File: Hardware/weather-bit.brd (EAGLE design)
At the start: 68.6 x 58.4 mm, 73 parts, among them J10 SMD, J2 RJ11, J3 RJ11, J8 Qwiic (vertical), J9 SMD, U1 BME280, U2 micro:bit

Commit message: run of checklist
- vector font in sch
- added testpoints
- corrected measures
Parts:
- added TP1, TP13, TP14, TP19, TP2, TP3, TP4, TP5, TP8, TP9: (no value), SparkFun-Connectors:TP_15TH
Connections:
- removed net 10: U2.P$16
- removed net 11: U2.P$17
- removed net 3: U2.P$1
- removed net 4: U2.P$6
- removed net 5: U2.P$7
- removed net 6: U2.P$8
- removed net 7: U2.P$9
- removed net 9: U2.P$15
- removed net N$3: U2.P$23
- net 3.3V: now also TP1.P$1
- net GND: now also TP2.P$1
- net RAIN: now also TP8.P$1
- net SCL: now also TP4.P$1
- net SDA: now also TP3.P$1
- net SOIL_DAT: now also TP19.P$1
- net SOIL_PWR: now also TP5.P$1
- net TEMP_DAT: now also TP9.P$1
- net WDIR: now also TP14.P$1
- net WSPEED: now also TP13.P$1
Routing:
- net SOIL_DAT: track 67.0 -> 77.2 mm
- net SCL: track 36.2 -> 44.2 mm
- net SDA: track 36.9 -> 43.8 mm
- net SOIL_PWR: track 52.9 -> 57.3 mm
- net TEMP_DAT: track 60.7 -> 65.1 mm
- net WSPEED: track 53.9 -> 57.8 mm
- net WDIR: track 50.2 -> 54.0 mm
- net RAIN: track 51.7 -> 55.6 mm
- net 3.3V: track 196.1 -> 200.0 mm
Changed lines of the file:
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@@
 <text x="31.75" y="-11.43" size="1.778" layer="51" font="vector" ratio="9">Mary West, based on Weather Shield Design by Nathan Seidle </text>
 <text x="67.16395" y="18.07845" size="1.778" layer="16" font="vector" ratio="15" rot="SMR270" align="center">v11</text>
-<text x="30.63875" y="90.4875" size="1.778" layer="47" font="vector" ratio="15">* All dimensions
+<text x="30.63875" y="81.5975" size="1.778" layer="47" font="vector" ratio="15">* All dimensions
   are in inches</text>
 <wire x1="2.54" y1="58.42" x2="66.04" y2="58.42" width="0.2032" layer="20"/>
@@
 <wire x1="68.58" y1="55.88" x2="68.58" y2="2.54" width="0.2032" layer="20"/>
 <wire x1="2.54" y1="58.42" x2="0" y2="55.88" width="0.2032" layer="20" curve="90"/>
-<dimension x1="68.58" y1="2.54" x2="68.58" y2="67.31" x3="85.09" y3="34.925" textsize="1.778" layer="47" unit="inch"/>
-<dimension x1="68.58" y1="67.31" x2="0" y2="67.31" x3="34.29" y3="81.5975" textsize="1.778" layer="47" unit="inch"/>
+<dimension x1="68.58" y1="2.54" x2="68.58" y2="58.42" x3="85.09" y3="30.48" textsize="1.778" layer="47" unit="inch"/>
+<dimension x1="68.58" y1="58.42" x2="0" y2="58.42" x3="34.29" y3="72.7075" textsize="1.778" layer="47" unit="inch"/>
 <wire x1="43.60545" y1="36.2204" x2="43.60545" y2="31.8516" width="0.254" layer="21"/>
 <wire x1="43.60545" y1="31.8516" x2="50.64125" y2="31.877" width="0.254" layer="21"/>
@@
 <wire x1="2.54" y1="0" x2="0" y2="2.54" width="0.2032" layer="20" curve="-90"/>
 <wire x1="0" y1="2.54" x2="0" y2="55.88" width="0.2032" layer="20"/>
-<dimension x1="2.54" y1="64.77" x2="66.04" y2="64.77" x3="34.29" y3="73.3425" textsize="1.778" textratio="15" layer="47" unit="inch"/>
-<dimension x1="66.04" y1="64.77" x2="66.04" y2="2.54" x3="75.2475" y3="33.655" textsize="1.778" textratio="15" layer="47" unit="inch"/>
+<dimension x1="2.54" y1="55.88" x2="66.04" y2="55.88" x3="34.29" y3="64.4525" textsize="1.778" textratio="15" layer="47" unit="inch"/>
+<dimension x1="66.04" y1="55.88" x2="66.04" y2="2.54" x3="75.2475" y3="29.21" textsize="1.778" textratio="15" layer="47" unit="inch"/>
 <dimension x1="66.04" y1="2.54" x2="67.78625" y2="2.54" x3="66.913125" y3="-2.06375" textsize="1.778" layer="47" unit="inch"/>
-<dimension x1="2.54" y1="64.77" x2="0.79375" y2="64.77" x3="1.666875" y3="69.5325" textsize="1.778" layer="47" unit="inch"/>
+<dimension x1="2.54" y1="55.88" x2="0.79375" y2="55.88" x3="1.666875" y3="60.6425" textsize="1.778" layer="47" unit="inch"/>
 <text x="6.223" y="-32.385" size="2.54" layer="51">Solder Mask: Black Gloss</text>
 <text x="11.43" y="-13.97" size="1.778" layer="51" font="vector">Revised by:</text>
@@
 <element name="U$33" library="buzzard_labels" package="SPARKFUN#COM#MICROBIT17" value="" x="49.1744" y="15.7226" smashed="yes" rot="MR0"/>
 <element name="U$34" library="buzzard_labels (1)" package="ALT0" value="" x="51.6382" y="36.3728" smashed="yes" rot="R270"/>
+<element name="TP1" library="SparkFun-Connectors" package="TP_15TH" value="" x="41.91" y="49.53" smashed="yes" rot="R90"/>
+<element name="TP2" library="SparkFun-Connectors" package="TP_15TH" value="" x="49.53" y="49.53" smashed="yes" rot="R90"/>
+<element name="TP3" library="SparkFun-Connectors" package="TP_15TH" value="" x="46.99" y="49.53" smashed="yes" rot="R90"/>
+<element name="TP4" library="SparkFun-Connectors" package="TP_15TH" value="" x="44.45" y="49.53" smashed="yes" rot="R90"/>
+<element name="TP5" library="SparkFun-Connectors" package="TP_15TH" value="" x="39.37" y="49.53" smashed="yes" rot="R90"/>
+<element name="TP8" library="SparkFun-Connectors" package="TP_15TH" value="" x="31.75" y="49.53" smashed="yes" rot="R90"/>
+<element name="TP9" library="SparkFun-Connectors" package="TP_15TH" value="" x="29.21" y="49.53" smashed="yes" rot="R90"/>
+<element name="TP13" library="SparkFun-Connectors" package="TP_15TH" value="" x="26.67" y="49.53" smashed="yes" rot="R90"/>
+<element name="TP14" library="SparkFun-Connectors" package="TP_15TH" value="" x="24.13" y="49.53" smashed="yes" rot="R90"/>
+<element name="TP19" library="SparkFun-Connectors" package="TP_15TH" value="" x="21.59" y="49.53" smashed="yes" rot="R90"/>
 </elements>
 <signals>
@@
 <wire x1="4.7234" y1="30.3022" x2="1.4234" y2="30.3022" width="0.254" layer="1"/>
 <wire x1="1.4234" y1="30.3022" x2="1.4234" y2="27.7622" width="0.254" layer="1"/>
+<contactref element="TP2" pad="P$1"/>
 </signal>
 <signal name="3.3V">
@@
 <wire x1="54.5976" y1="33.1678" x2="49.73405" y2="33.1678" width="0.508" layer="1"/>
 <wire x1="49.70145" y1="33.1352" x2="49.73405" y2="33.1678" width="0.508" layer="1"/>
+<contactref element="TP1" pad="P$1"/>
+<wire x1="42.545" y1="45.92" x2="42.545" y2="48.895" width="0.2032" layer="1"/>
+<wire x1="42.545" y1="48.895" x2="41.91" y2="49.53" width="0.2032" layer="1"/>
 </signal>
 <signal name="N$2">
@@
 <wire x1="63.8312" y1="32.0294" x2="63.7794" y2="32.0294" width="0.254" layer="1"/>
 <wire x1="63.7794" y1="32.0294" x2="63.641" y2="32.1678" width="0.254" layer="1"/>
+<contactref element="TP3" pad="P$1"/>
+<wire x1="51.435" y1="45.92" x2="51.435" y2="47.625" width="0.2032" layer="1"/>
+<wire x1="51.435" y1="47.625" x2="50.8" y2="48.26" width="0.2032" layer="1"/>
+<wire x1="50.8" y1="48.26" x2="48.26" y2="48.26" width="0.2032" layer="1"/>
+<wire x1="48.26" y1="48.26" x2="46.99" y2="49.53" width="0.2032" layer="1"/>
 </signal>
 <signal name="SCL">
@@
 <wire x1="67.1312" y1="30.227" x2="66.9036" y2="30.4546" width="0.254" layer="1"/>
 <wire x1="66.9036" y1="30.4546" x2="60.9854" y2="30.4546" width="0.254" layer="1"/>
+<contactref element="TP4" pad="P$1"/>
+<wire x1="50.165" y1="45.92" x2="50.165" y2="47.3456" width="0.2032" layer="1"/>
+<wire x1="49.8094" y1="47.7012" x2="46.2788" y2="47.7012" width="0.2032" layer="1"/>
+<wire x1="46.2788" y1="47.7012" x2="44.45" y2="49.53" width="0.2032" layer="1"/>
+<wire x1="50.165" y1="47.3456" x2="49.8094" y2="47.7012" width="0.2032" layer="1"/>
 </signal>
 <signal name="N$5">
@@
 <wire x1="32.0675" y1="24.765" x2="31.115" y2="25.7175" width="0.254" layer="1"/>
 <wire x1="31.115" y1="25.7175" x2="31.115" y2="45.92" width="0.254" layer="1"/>
+<contactref element="TP9" pad="P$1"/>
+<wire x1="31.115" y1="45.92" x2="31.115" y2="47.625" width="0.2032" layer="1"/>
+<wire x1="31.115" y1="47.625" x2="29.21" y2="49.53" width="0.2032" layer="1"/>
 </signal>
 <signal name="SOIL_PWR">
@@
 <contactref element="U2" pad="P$26"/>
 <wire x1="41.275" y1="45.92" x2="41.275" y2="42.8625" width="0.254" layer="1"/>
+<contactref element="TP5" pad="P$1"/>
+<wire x1="41.275" y1="45.92" x2="41.275" y2="47.625" width="0.2032" layer="1"/>
+<wire x1="41.275" y1="47.625" x2="39.37" y2="49.53" width="0.2032" layer="1"/>
 </signal>
 <signal name="SOIL_DAT">
@@
 <wire x1="12.065" y1="43.815" x2="13.335" y2="43.815" width="0.254" layer="1"/>
 <wire x1="12.065" y1="45.92" x2="12.065" y2="43.815" width="0.254" layer="1"/>
+<contactref element="TP19" pad="P$1"/>
+<wire x1="14.605" y1="45.92" x2="14.605" y2="48.895" width="0.2032" layer="1"/>
+<wire x1="14.605" y1="48.895" x2="15.24" y2="49.53" width="0.2032" layer="1"/>
+<wire x1="15.24" y1="49.53" x2="21.59" y2="49.53" width="0.2032" layer="1"/>
 </signal>
 <signal name="RAIN">
@@
 <wire x1="33.655" y1="45.92" x2="33.655" y2="43.688" width="0.254" layer="1"/>
 <wire x1="34.925" y1="45.92" x2="34.925" y2="43.688" width="0.254" layer="1"/>
+<contactref element="TP8" pad="P$1"/>
+<wire x1="32.385" y1="45.92" x2="32.385" y2="48.895" width="0.2032" layer="1"/>
+<wire x1="32.385" y1="48.895" x2="31.75" y2="49.53" width="0.2032" layer="1"/>
 </signal>
 <signal name="WDIR">
@@
 <wire x1="22.225" y1="45.92" x2="22.225" y2="43.7261" width="0.254" layer="1"/>
 <wire x1="23.495" y1="45.92" x2="23.495" y2="43.7261" width="0.254" layer="1"/>
+<contactref element="TP14" pad="P$1"/>
+<wire x1="24.765" y1="45.92" x2="24.765" y2="48.895" width="0.2032" layer="1"/>
+<wire x1="24.765" y1="48.895" x2="24.13" y2="49.53" width="0.2032" layer="1"/>
 </signal>
 <signal name="WSPEED">
@@
 <wire x1="17.78" y1="21.17" x2="17.78" y2="22.5425" width="0.254" layer="1"/>
 <wire x1="17.78" y1="22.5425" x2="18.0975" y2="22.86" width="0.254" layer="1"/>
-<wire x1="26.44775" y1="22.86" x2="26.67" y2="22.86" width="0.254" layer="1"/>
-<wire x1="26.67" y1="22.86" x2="38.1" y2="22.86" width="0.254" layer="1"/>
+<wire x1="26.035" y1="22.86" x2="38.1" y2="22.86" width="0.254" layer="1"/>
 <wire x1="38.1" y1="22.86" x2="40.64" y2="22.86" width="0.254" layer="1"/>
 <wire x1="40.64" y1="22.86" x2="41.91" y2="21.59" width="0.254" layer="1"/>
@@
 <contactref element="U2" pad="P$14"/>
 <wire x1="26.035" y1="45.92" x2="26.035" y2="22.86" width="0.254" layer="1"/>
-<wire x1="26.44775" y1="22.86" x2="26.035" y2="22.86" width="0.254" layer="1"/>
+<contactref element="TP13" pad="P$1"/>
+<wire x1="26.035" y1="45.92" x2="26.035" y2="48.895" width="0.2032" layer="1"/>
+<wire x1="26.035" y1="48.895" x2="26.67" y2="49.53" width="0.2032" layer="1"/>
 </signal>
 <signal name="N$1">
@@
 <wire x1="4.7234" y1="37.9222" x2="4.7244" y2="37.9212" width="0.254" layer="1"/>
 </signal>
-<signal name="11">
-<contactref element="U2" pad="P$17"/>
-</signal>
-<signal name="10">
-<contactref element="U2" pad="P$16"/>
-</signal>
-<signal name="7">
-<contactref element="U2" pad="P$9"/>
-</signal>
-<signal name="6">
-<contactref element="U2" pad="P$8"/>
-</signal>
-<signal name="5">
-<contactref element="U2" pad="P$7"/>
-</signal>
-<signal name="4">
-<contactref element="U2" pad="P$6"/>
-</signal>
-<signal name="3">
-<contactref element="U2" pad="P$1"/>
-</signal>
-<signal name="9">
-<contactref element="U2" pad="P$15"/>
-</signal>
-<signal name="N$3">
-<contactref element="U2" pad="P$23"/>
-</signal>
 </signals>

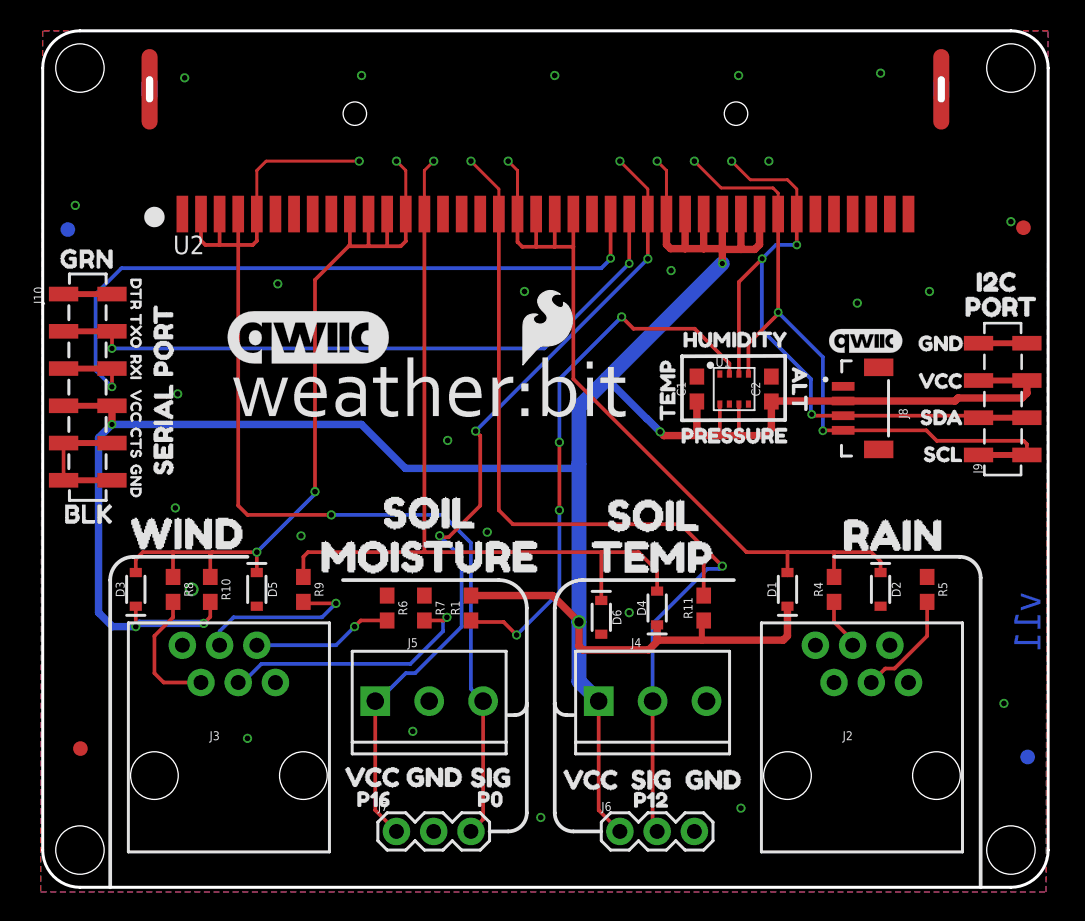
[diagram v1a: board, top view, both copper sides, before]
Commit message: switched to TIGHT DRC, nudging and routing
-updated package on 4-pin SMD to allow for routing to either pad under each header
-moved to TIGHT DRC, some slight nudging of routes to comply
-rotated SERIAL PORT silk to match pin labels
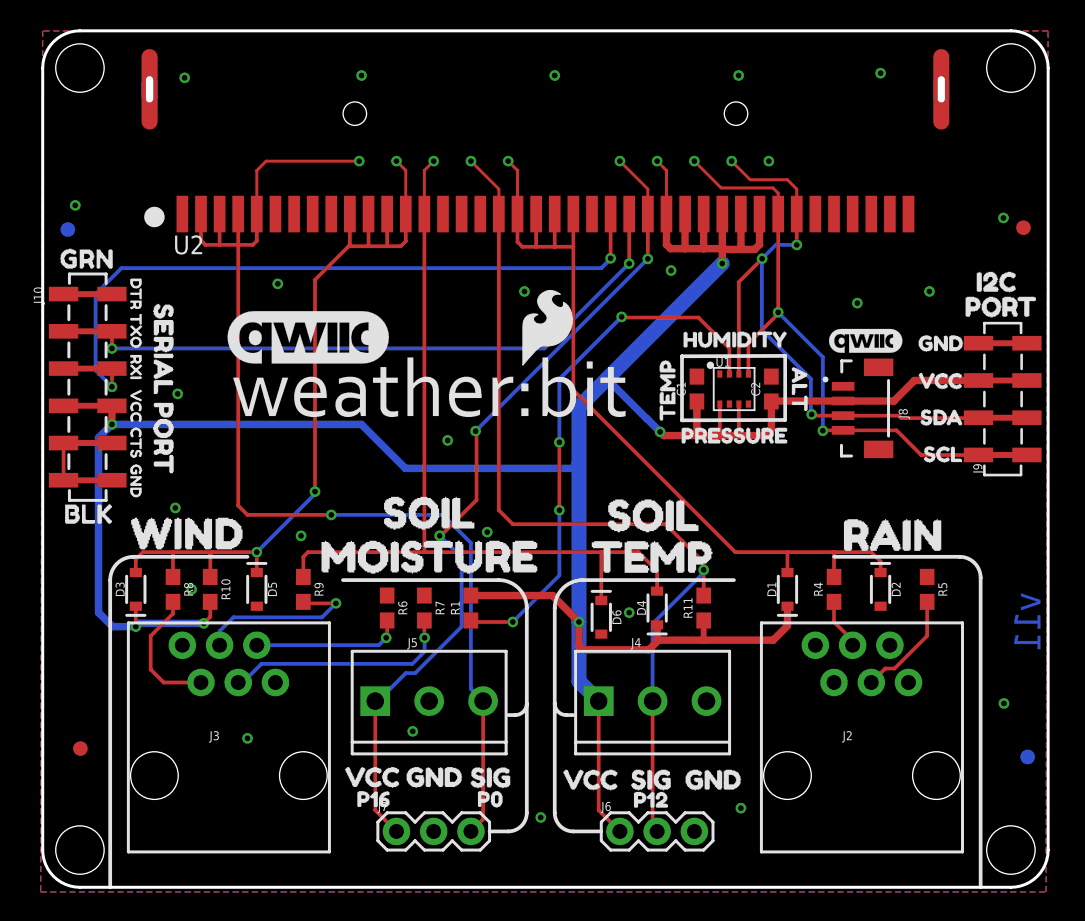
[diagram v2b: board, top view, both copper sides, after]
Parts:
- J9: value SMD -> 1X04_SMD_STRAIGHT_COMBO
- moved U$10 14.0 mm to (8.26, 40.9), turned to 270 degrees
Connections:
- net 3.3V: now also J9.3-2
- net GND: now also J9.4-2
- net SCL: now also J9.1-2
- net SDA: now also J9.2-2
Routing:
- net SDA: track 43.8 -> 47.2 mm
- net GND: track 5.84 -> 9.14 mm
- net TEMP_DAT: track 65.1 -> 61.8 mm
- net N$14: track 18.1 -> 15.7 mm
- net 3.3V: track 200.0 -> 198.9 mm
- net N$2: track 37.6 -> 36.8 mm
- net N$13: track 9.59 -> 10.2 mm
- net SOIL_PWR: track 57.3 -> 56.7 mm

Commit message: Finalized test points and test point positions
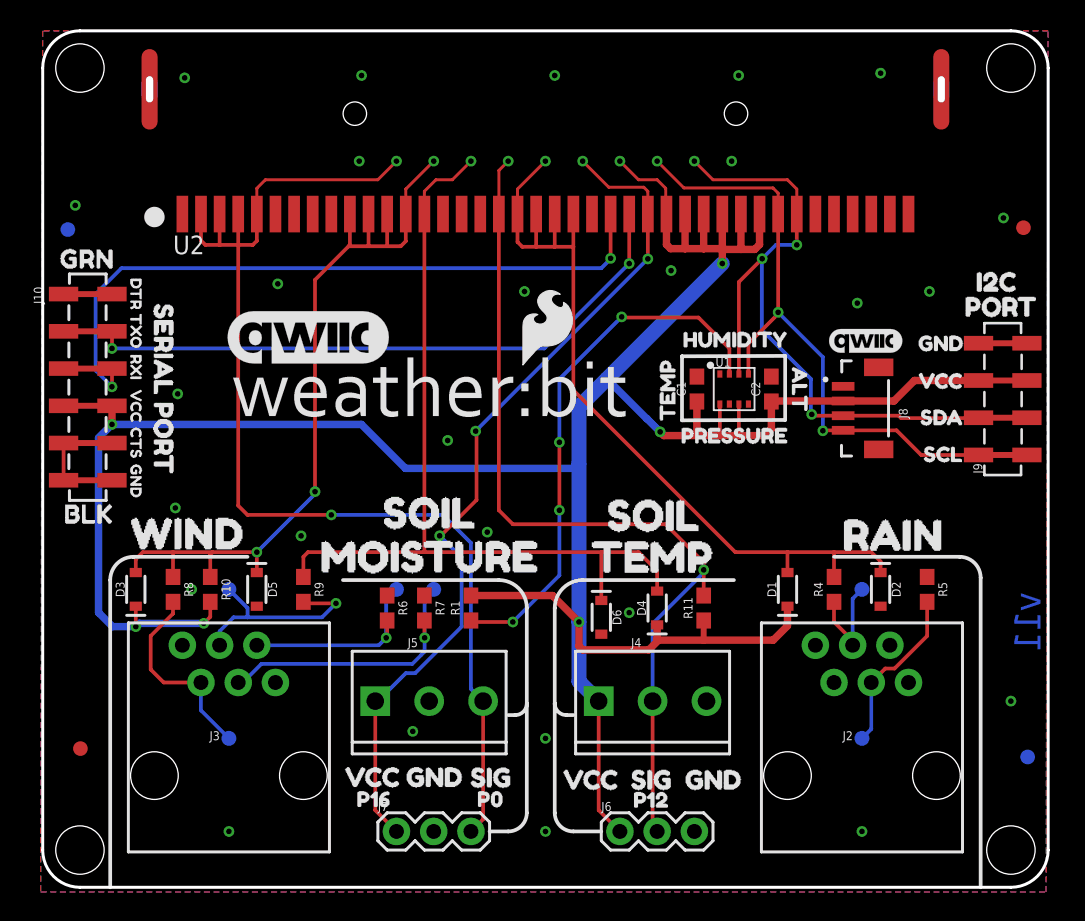
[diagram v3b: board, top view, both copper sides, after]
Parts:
- added TP10, TP11, TP12, TP15, TP6, TP7: (no value), SparkFun-Connectors:PAD.03X.04
- added TP16, TP17: (no value), SparkFun-Connectors:TP_15TH
- moved TP4 2.54 mm to (41.9, 49.5)
- moved TP14 2.54 mm to (26.7, 49.5)
- moved TP1 2.54 mm to (39.4, 49.5)
- moved TP13 2.54 mm to (29.2, 49.5)
- moved TP19 2.54 mm to (24.1, 49.5)
- moved TP2 2.54 mm to (47.0, 49.5)
- moved TP3 2.54 mm to (44.5, 49.5)
- moved TP5 2.54 mm to (36.8, 49.5)
- moved TP8 2.54 mm to (34.3, 49.5)
- moved TP9 2.54 mm to (31.8, 49.5)
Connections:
- removed net N$11: J3.3, R9.2
- removed net N$13: J3.5, R6.2
- removed net N$14: J3.4, R7.2
- removed net N$5: J2.3, R4.1
- removed net N$6: J3.2, R8.2
- removed net N$7: J2.4, R5.2
- new net RAIN_PIN_3: J2.3, R4.1, TP6.P$1
- new net RAIN_PIN_4: J2.4, R5.2, TP7.P$1
- new net WIND_PIN_2: J3.2, R8.2, TP10.P$1
- new net WIND_PIN_3: J3.3, R9.2, TP11.P$1
- new net WIND_PIN_4: J3.4, R7.2, TP12.P$1
- new net WIND_PIN_5: J3.5, R6.2, TP15.P$1
- net GND: now also TP16.P$1, TP17.P$1
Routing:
- net WIND_PIN_4: track 0.00 -> 19.3 mm, vias 0 -> 1
- net N$14: track 15.7 -> 0.00 mm, vias 1 -> 0
- net WIND_PIN_3: track 0.00 -> 14.4 mm, vias 0 -> 1
- net WIND_PIN_5: track 0.00 -> 13.8 mm, vias 0 -> 1
- net WIND_PIN_2: track 0.00 -> 13.6 mm
- net N$11: track 11.9 -> 0.00 mm, vias 1 -> 0
- net RAIN_PIN_4: track 0.00 -> 11.5 mm
- net N$13: track 10.2 -> 0.00 mm, vias 1 -> 0
- net N$6: track 9.04 -> 0.00 mm
- net RAIN_PIN_3: track 0.00 -> 7.56 mm
- net N$7: track 7.45 -> 0.00 mm
- net N$5: track 3.49 -> 0.00 mm
- net SDA: track 47.2 -> 49.7 mm
- net SCL: track 43.8 -> 46.3 mm
- net SOIL_PWR: track 56.7 -> 59.1 mm
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
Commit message: Connected TEMP_DATA to P13
On v10, TEMP_DATA was connected to both P12 and P13 (for the one-wire interface to the temp sensor).

v11 only had TEMP_DATA connected to P12.

With this commit (v12), TEMP_DATA is connected to both P12 and P13 (to match the original v10).

Also incremented version to v12 in BRD and SCH.
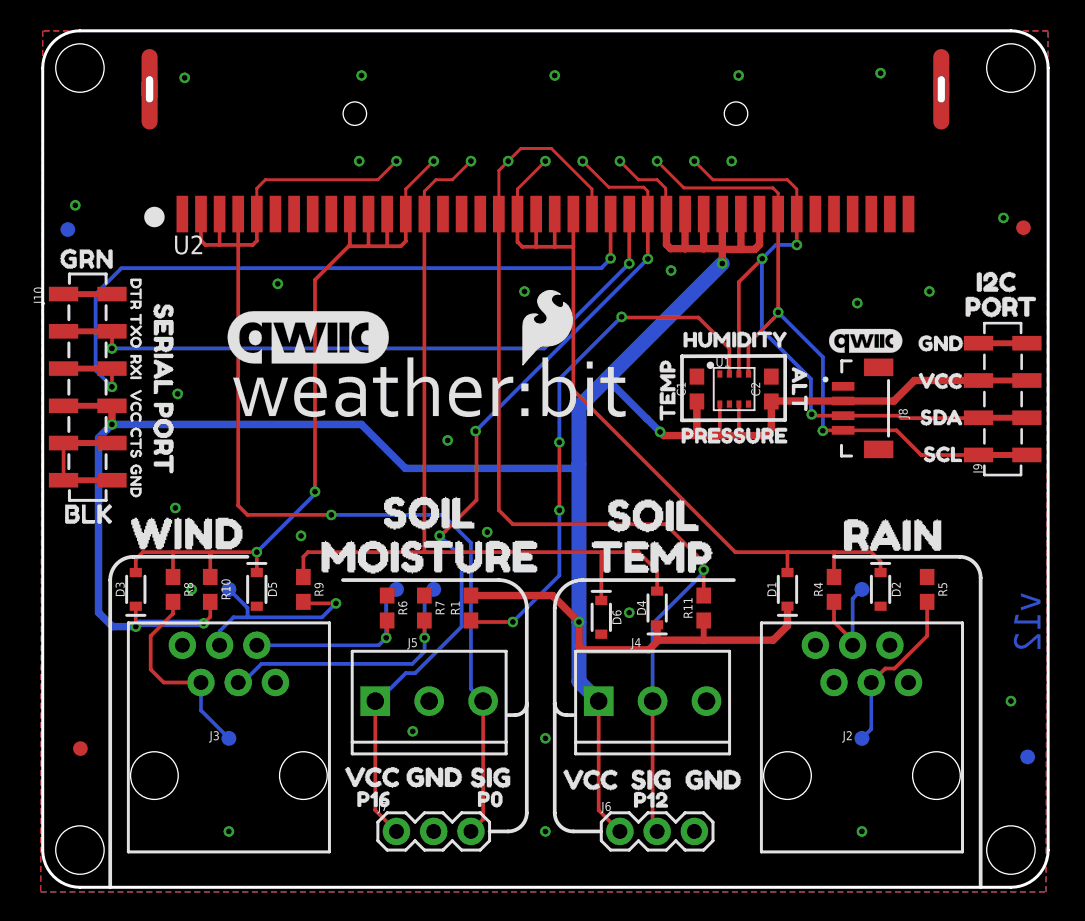
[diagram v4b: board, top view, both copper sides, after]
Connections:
- net TEMP_DAT: now also U2.P$23
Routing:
- net TEMP_DAT: track 61.3 -> 70.2 mm
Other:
- board text added: "v12"
- board text removed: "v11"
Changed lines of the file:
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@@
 <plain>
 <text x="31.75" y="-11.43" size="1.778" layer="51" font="vector" ratio="9">Mary West, based on Weather Shield Design by Nathan Seidle </text>
-<text x="67.16395" y="18.07845" size="1.778" layer="16" font="vector" ratio="15" rot="SMR270" align="center">v11</text>
+<text x="67.16395" y="18.07845" size="1.778" layer="16" font="vector" ratio="15" rot="SMR270" align="center">v12</text>
 <text x="30.63875" y="81.5975" size="1.778" layer="47" font="vector" ratio="15">* All dimensions
   are in inches</text>
@@
 <wire x1="42.4815" y1="24.765" x2="45.085" y2="22.1615" width="0.254" layer="1"/>
 <wire x1="45.085" y1="22.1615" x2="45.085" y2="21.6535" width="0.254" layer="1"/>
+<contactref element="U2" pad="P$23"/>
+<wire x1="37.465" y1="45.92" x2="37.465" y2="47.625" width="0.2032" layer="1"/>
+<wire x1="34.6964" y1="50.3936" x2="32.6136" y2="50.3936" width="0.2032" layer="1"/>
+<wire x1="32.6136" y1="50.3936" x2="31.75" y2="49.53" width="0.2032" layer="1"/>
+<wire x1="37.465" y1="47.625" x2="34.6964" y2="50.3936" width="0.2032" layer="1"/>
 </signal>
 <signal name="SOIL_PWR">
